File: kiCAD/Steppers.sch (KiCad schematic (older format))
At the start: 114 parts, among them J4 X, J5 E0, J6 Y, J7 E1, J8 Z, J9 E2, U4 TMC2209, U5 TMC2209, U6 TMC2209, U7 TMC2209, U8 TMC2209, U9 TMC2209

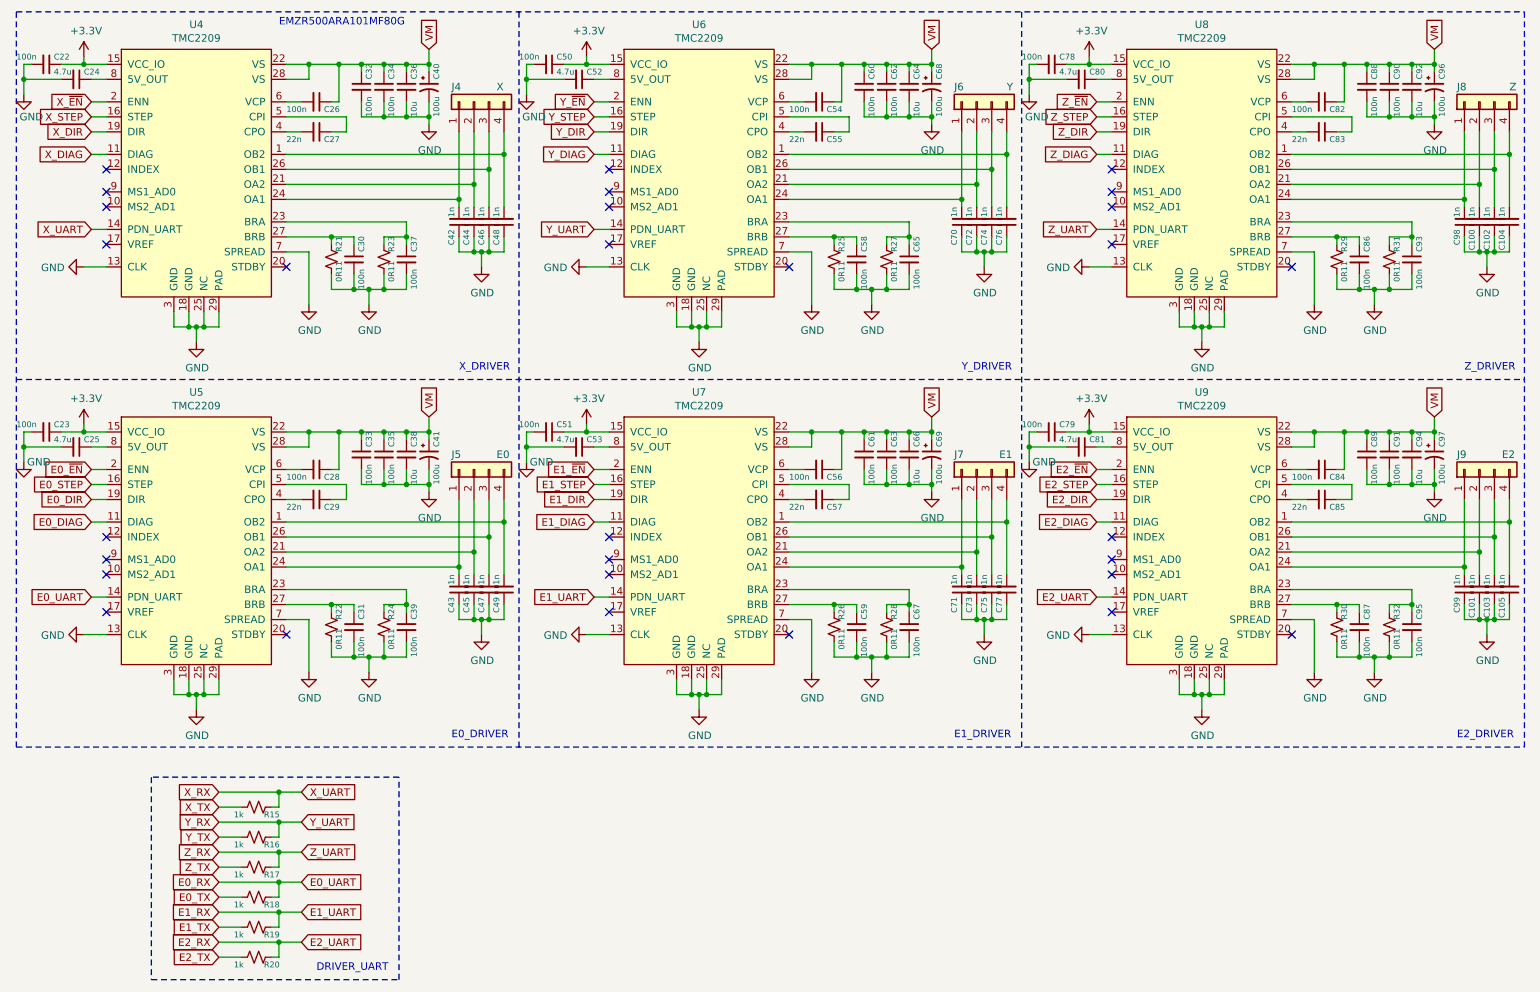
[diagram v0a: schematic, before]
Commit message: layed out TMC's and started laying out power electronics
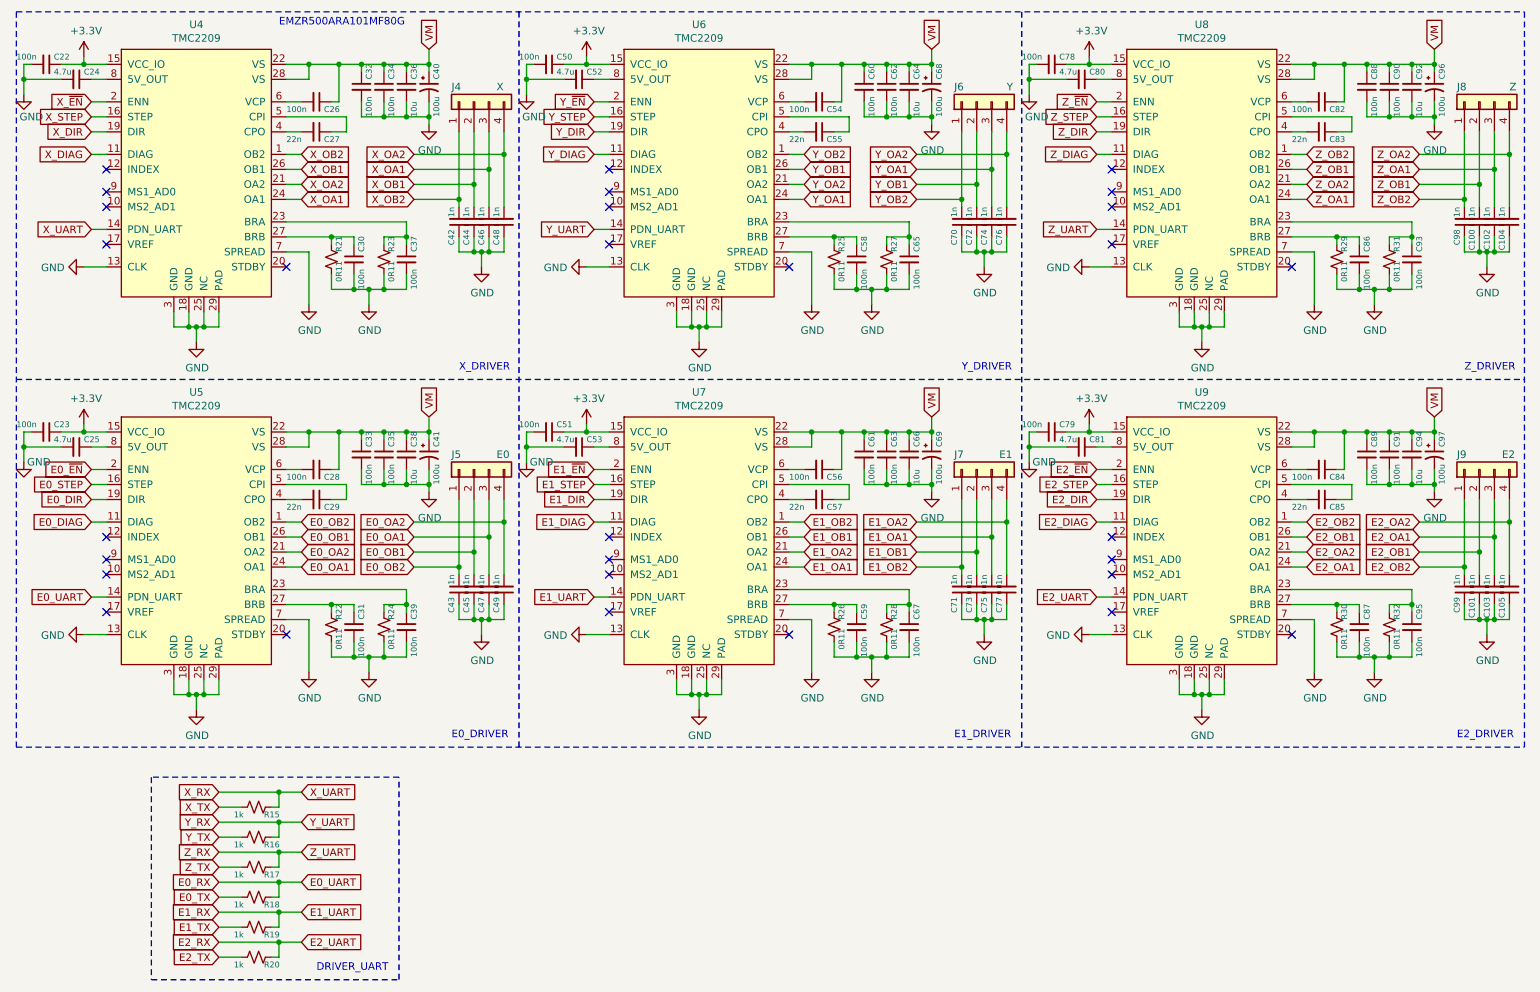
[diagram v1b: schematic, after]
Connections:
- net X_OA2: now reaches C48.2, J4.4 (Pin_4)
- net X_OA2: now also U4.21 (OA2); no longer U4.1 (OB2)
- net X_OB1: now reaches C44.2, J4.2 (Pin_2)
- net X_OB1: now also U4.26 (OB1); no longer U4.21 (OA2)
- net X_OB2: now reaches C42.2, J4.1 (Pin_1)
- net X_OB2: now also U4.1 (OB2); no longer U4.24 (OA1)
- net X_OA1: now reaches C46.2, J4.3 (Pin_3)
- net X_OA1: now also U4.24 (OA1); no longer U4.26 (OB1)
- net Y_OA2: now reaches C76.2, J6.4 (Pin_4)
- net Y_OA2: now also U6.21 (OA2); no longer U6.1 (OB2)
- net Y_OB1: now reaches C72.2, J6.2 (Pin_2)
- net Y_OB1: now also U6.26 (OB1); no longer U6.21 (OA2)
- net Y_OB2: now reaches C70.2, J6.1 (Pin_1)
- net Y_OB2: now also U6.1 (OB2); no longer U6.24 (OA1)
- net Y_OA1: now reaches C74.2, J6.3 (Pin_3)
- net Y_OA1: now also U6.24 (OA1); no longer U6.26 (OB1)
- net Z_OA2: now reaches C104.2, J8.4 (Pin_4)
- net Z_OA2: now also U8.21 (OA2); no longer U8.1 (OB2)
- net Z_OB1: now reaches C100.2, J8.2 (Pin_2)
- net Z_OB1: now also U8.26 (OB1); no longer U8.21 (OA2)
- net Z_OB2: now reaches C98.2, J8.1 (Pin_1)
- net Z_OB2: now also U8.1 (OB2); no longer U8.24 (OA1)
- net Z_OA1: now reaches C102.2, J8.3 (Pin_3)
- net Z_OA1: now also U8.24 (OA1); no longer U8.26 (OB1)
- net E0_OA2: now reaches C49.2, J5.4 (Pin_4)
- net E0_OA2: now also U5.21 (OA2); no longer U5.1 (OB2)
- net E0_OB1: now reaches C45.2, J5.2 (Pin_2)
- net E0_OB1: now also U5.26 (OB1); no longer U5.21 (OA2)
- net E0_OB2: now reaches C43.2, J5.1 (Pin_1)
- net E0_OB2: now also U5.1 (OB2); no longer U5.24 (OA1)
- net E0_OA1: now reaches C47.2, J5.3 (Pin_3)
- net E0_OA1: now also U5.24 (OA1); no longer U5.26 (OB1)
- net E1_OA2: now reaches C77.2, J7.4 (Pin_4)
- net E1_OA2: now also U7.21 (OA2); no longer U7.1 (OB2)
- net E1_OB1: now reaches C73.2, J7.2 (Pin_2)
- net E1_OB1: now also U7.26 (OB1); no longer U7.21 (OA2)
- net E1_OB2: now reaches C71.2, J7.1 (Pin_1)
- net E1_OB2: now also U7.1 (OB2); no longer U7.24 (OA1)
- net E1_OA1: now reaches C75.2, J7.3 (Pin_3)
- net E1_OA1: now also U7.24 (OA1); no longer U7.26 (OB1)
- net E2_OA2: now reaches C105.2, J9.4 (Pin_4)
- net E2_OA2: now also U9.21 (OA2); no longer U9.1 (OB2)
- net E2_OB1: now reaches C101.2, J9.2 (Pin_2)
- net E2_OB1: now also U9.26 (OB1); no longer U9.21 (OA2)
- net E2_OB2: now reaches C99.2, J9.1 (Pin_1)
- net E2_OB2: now also U9.1 (OB2); no longer U9.24 (OA1)
- net E2_OA1: now reaches C103.2, J9.3 (Pin_3)
- net E2_OA1: now also U9.24 (OA1); no longer U9.26 (OB1)
